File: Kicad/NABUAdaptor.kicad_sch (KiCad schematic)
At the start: 103 parts, among them J1 Conn_01x04, J2 DIN-5_180degree, J3 Conn_01x09, J4 Conn_01x05, U1 74LS164, U10 UA9638CD, U11 UA9637, U12 74LS164, U13 74LS164, U14 74LS04, U15 74LS74, U16 N8X60, U17 2114, U18 2114, U19 LM339, U2 74LS30, U20 74LS164, U21 74LS86, U22 74LS74, U23 74LS00, U24 74LS04, U25 74LS00, U26 74LS74, U27 74LS00, U28 74LS74, U29 74LS74, U3 74LS27, U30 74LS02, U31 MC6805P2, U32 74LS74, U33 74HCU04, U4 74LS164, U5 PAL16R6 (ID PAL), U6 74LS374, U7 74LS373, U8 3k3, U9 TR1865PL, Y1 3.579545MHz

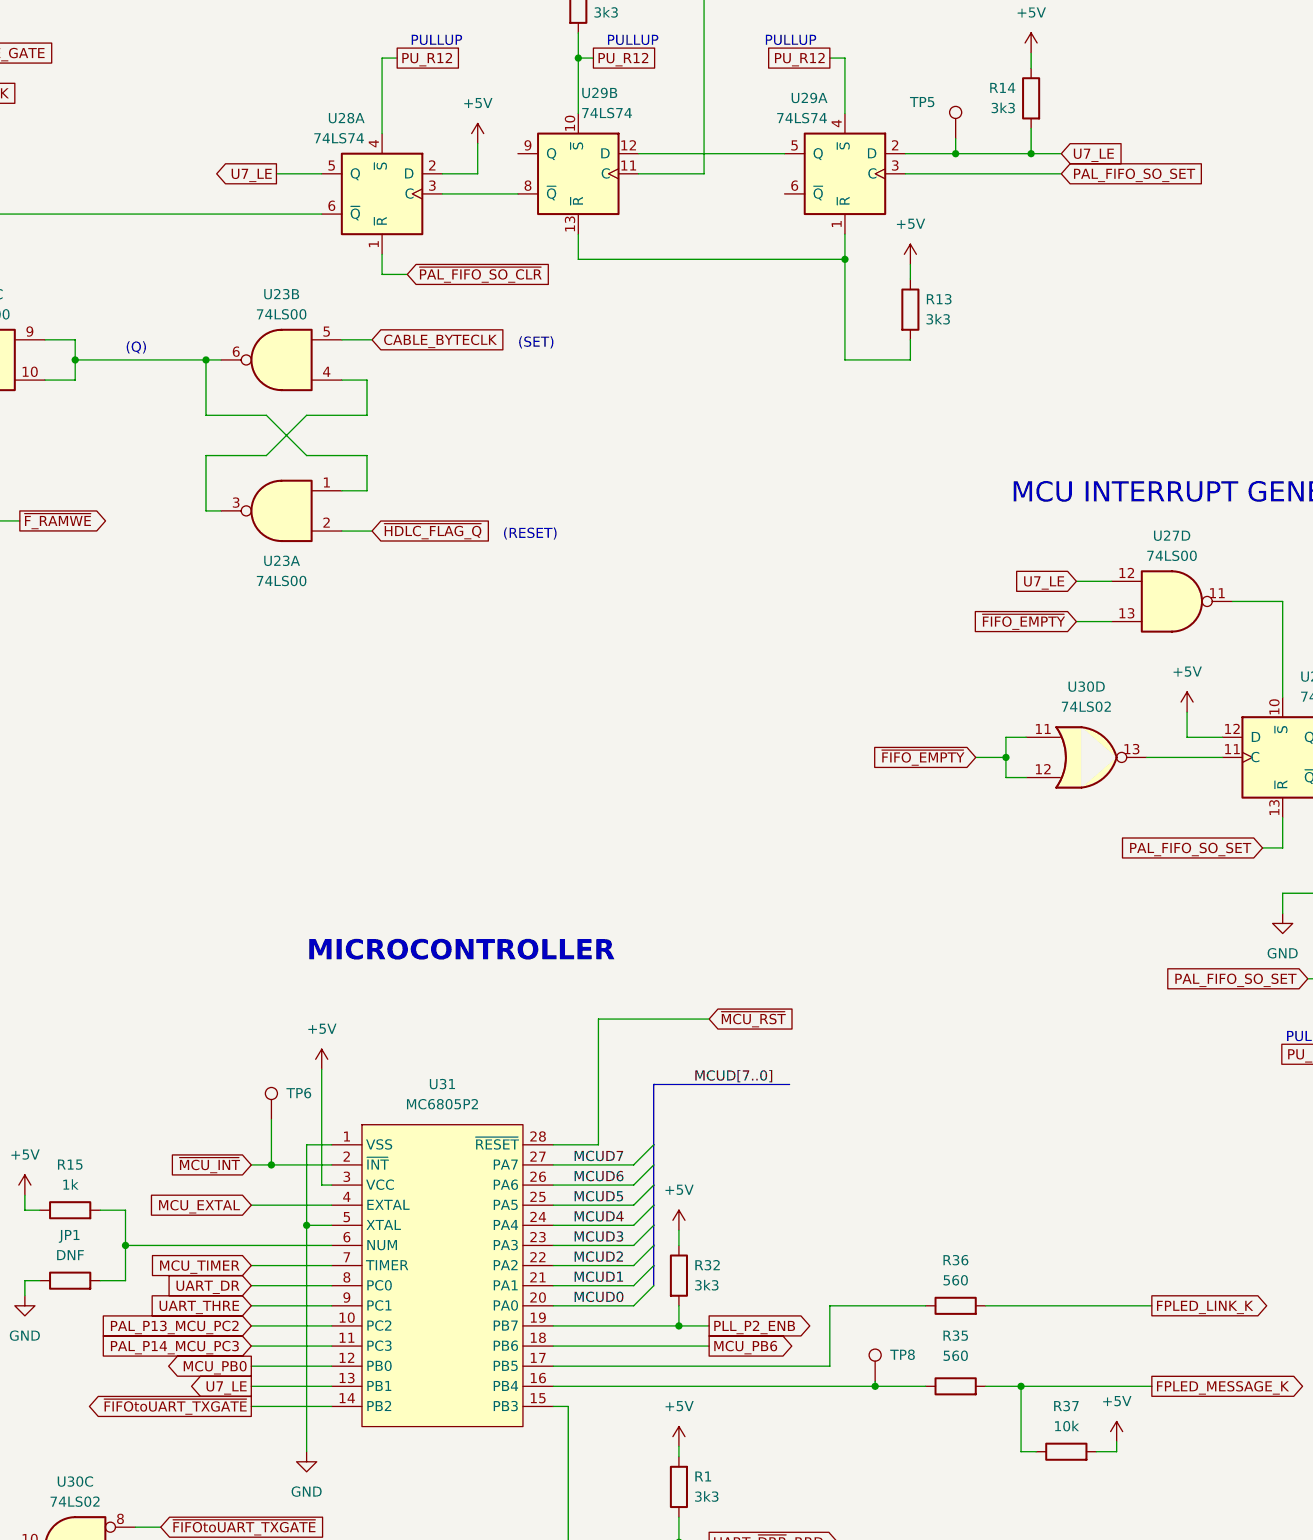
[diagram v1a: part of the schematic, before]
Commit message: schematic: Fix U7 OE wiring
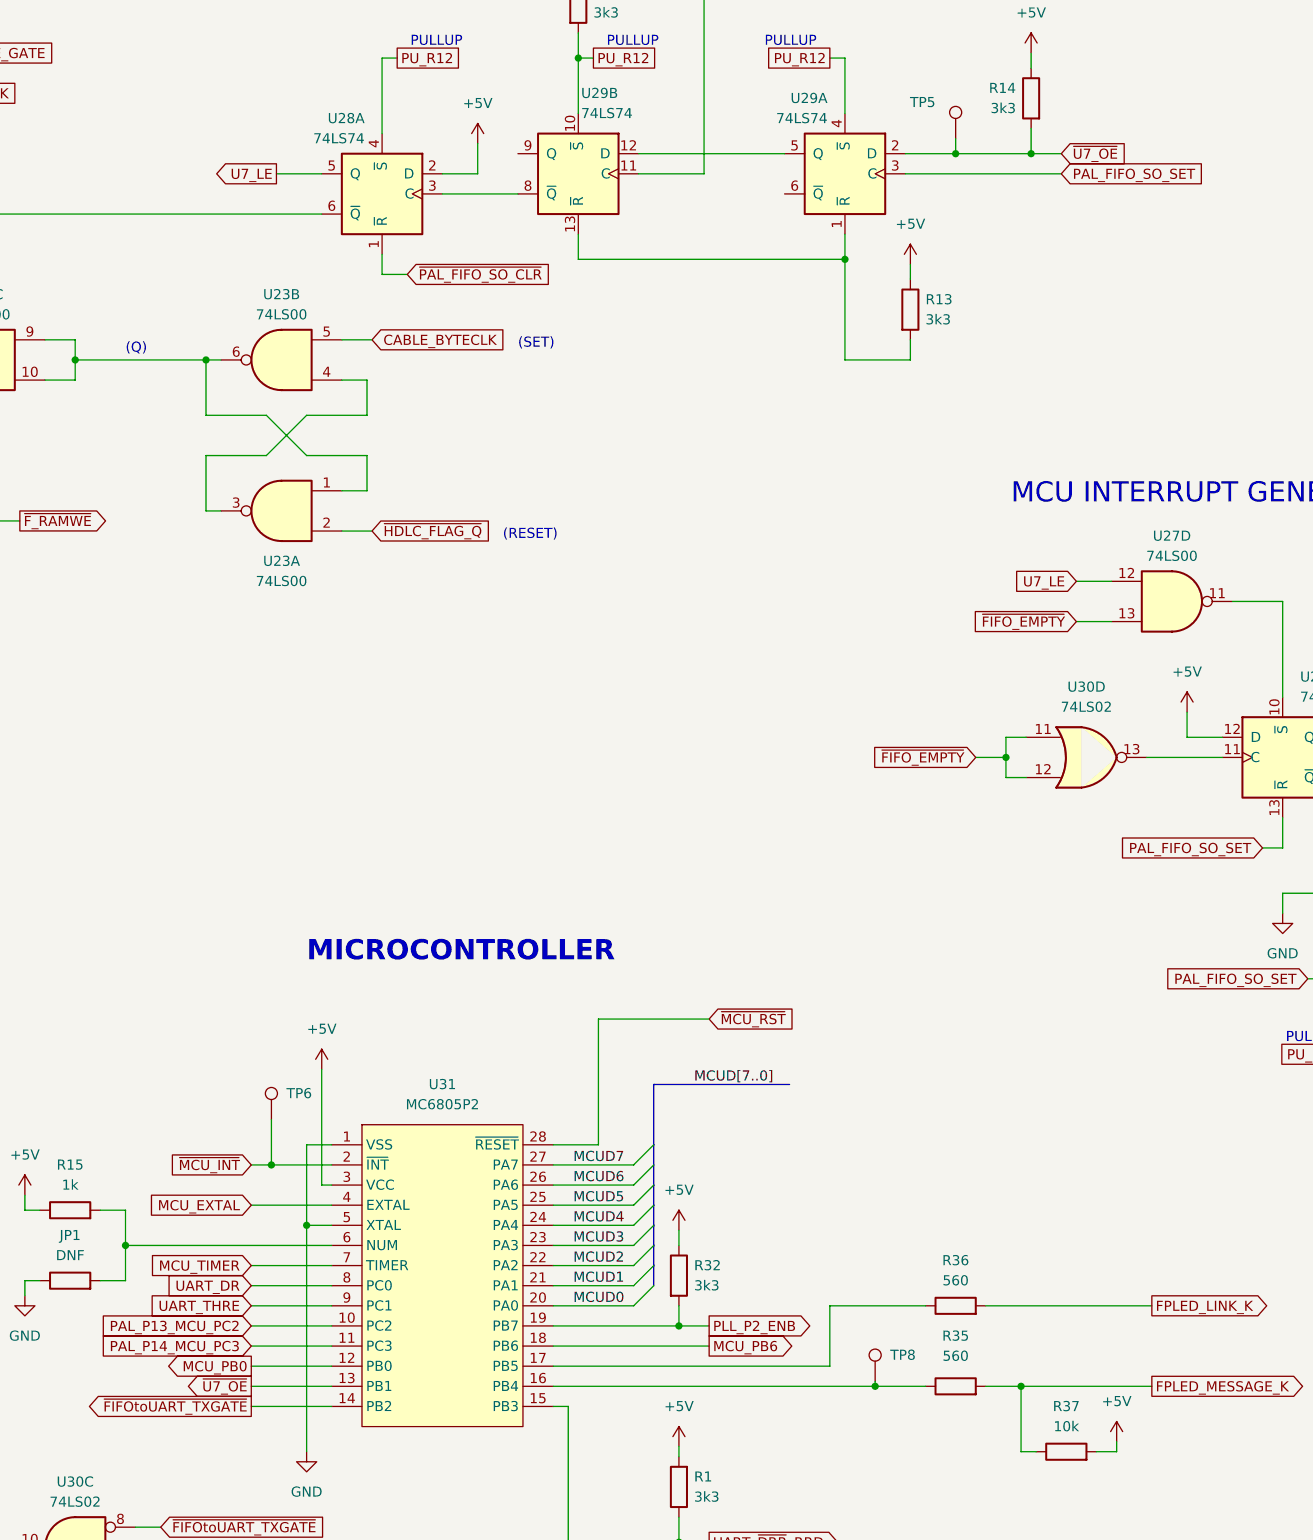
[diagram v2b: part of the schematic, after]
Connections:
- net U7_LE: no longer R14.2, TP5.1, U29.2 (D), U31.13 (PB1)
- net ~{U7_OE}: now also R14.2, TP5.1, U29.2 (D), U31.13 (PB1)
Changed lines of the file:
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@@
     )
   )
-  (global_label "U7_LE" (shape output) (at 419.1 423.545 180) (fields_autoplaced)
+  (global_label "~{U7_OE}" (shape output) (at 419.1 423.545 180) (fields_autoplaced)
     (effects (font (size 1.27 1.27)) (justify right))
-    (property "Intersheetrefs" "${INTERSHEET_REFS}" (at 410.4301 423.545 0)
+    (property "Intersheetrefs" "${INTERSHEET_REFS}" (at 410.1277 423.545 0)
       (effects (font (size 1.27 1.27)) (justify right))
     )
@@
     )
   )
-  (global_label "U7_LE" (shape input) (at 521.335 267.97 0) (fields_autoplaced)
+  (global_label "~{U7_OE}" (shape input) (at 521.335 267.97 0) (fields_autoplaced)
     (effects (font (size 1.27 1.27)) (justify left))
-    (property "Intersheetrefs" "${INTERSHEET_REFS}" (at 530.0049 267.97 0)
+    (property "Intersheetrefs" "${INTERSHEET_REFS}" (at 530.3073 267.97 0)
       (effects (font (size 1.27 1.27)) (justify left))
     )

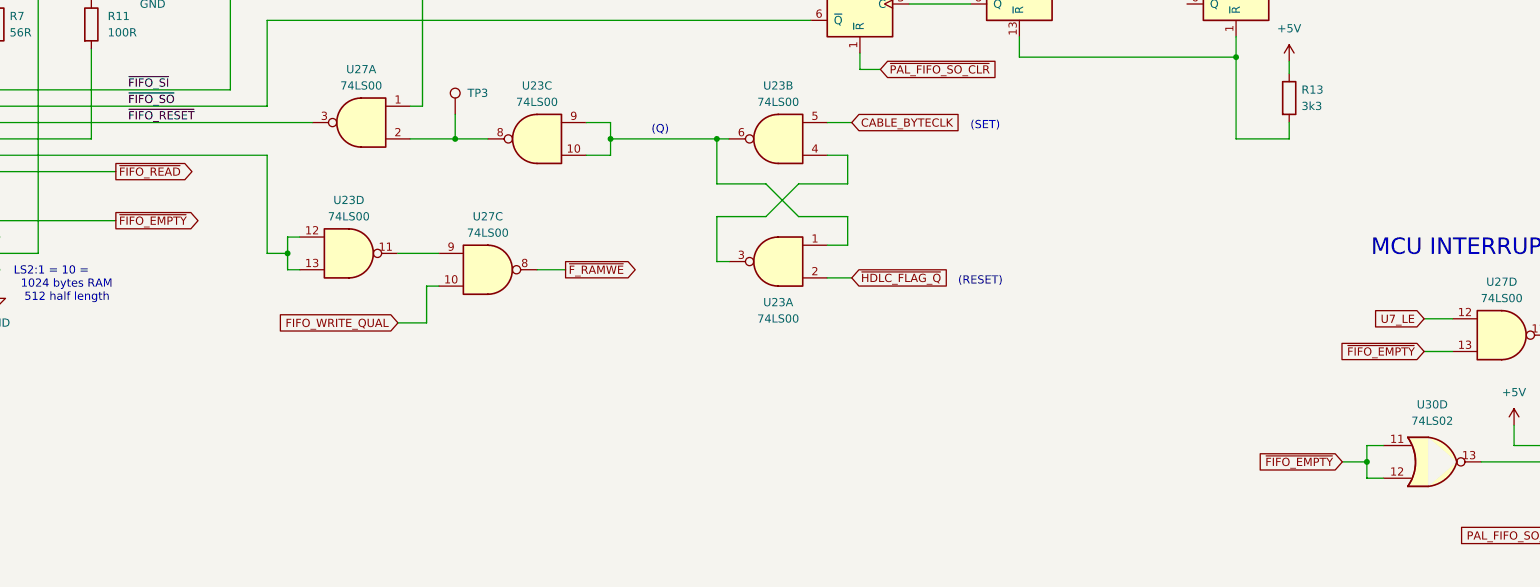
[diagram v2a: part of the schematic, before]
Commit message: schematic: fix signal polarities
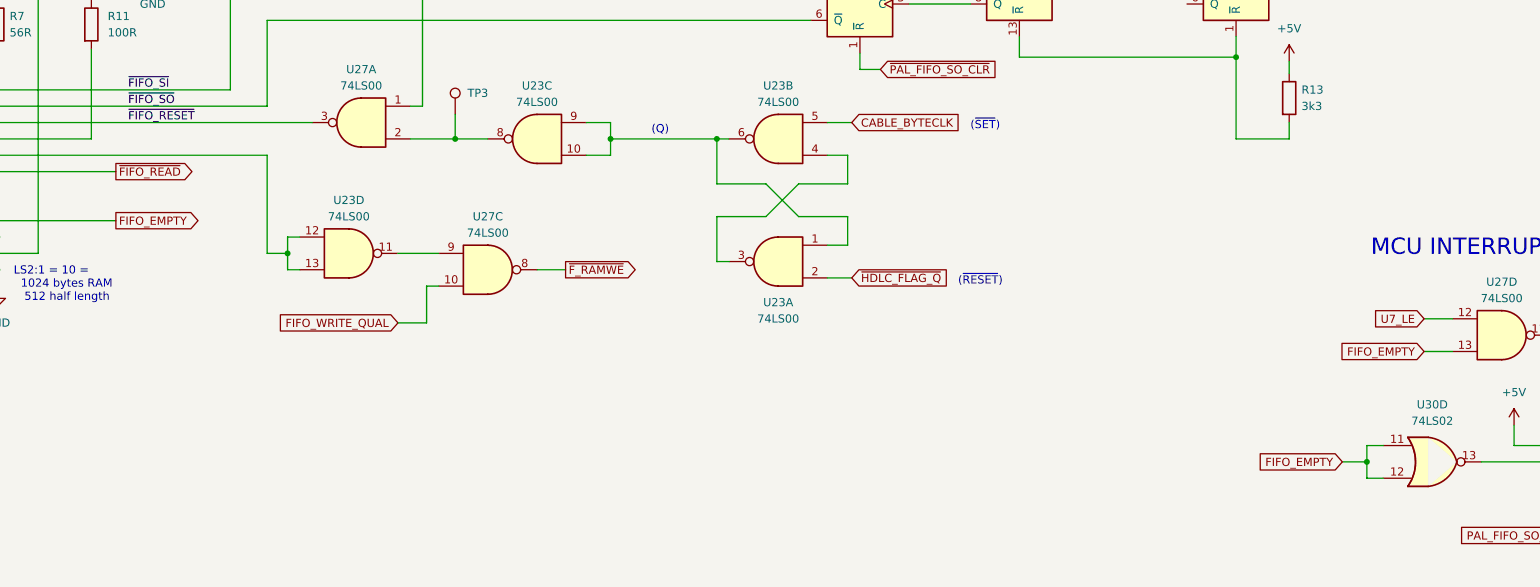
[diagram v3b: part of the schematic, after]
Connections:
- net ~{FIFO_EMPTY} renamed FIFO_EMPTY
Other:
- note added: "(~{RESET})"
- note added: "(~{SET})"
- note removed: "(RESET)"
- note removed: "(SET)"
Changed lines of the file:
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@@
     (effects (font (size 2.54 2.54)) (justify left bottom))
   )
-  (text "(RESET)" (at 450.85 316.865 0)
+  (text "(~{RESET})" (at 450.85 316.865 0)
     (effects (font (size 1.27 1.27)) (justify left bottom))
   )
@@
     (effects (font (size 2.54 2.54) (thickness 0.508) bold) (justify left bottom))
   )
-  (text "(SET)" (at 452.755 292.735 0)
+  (text "(~{SET})" (at 452.755 292.735 0)
     (effects (font (size 1.27 1.27)) (justify left bottom))
   )
@@
     )
   )
-  (global_label "~{FIFO_EMPTY}" (shape input) (at 523.24 327.025 180) (fields_autoplaced)
+  (global_label "FIFO_EMPTY" (shape input) (at 523.24 327.025 180) (fields_autoplaced)
     (effects (font (size 1.27 1.27)) (justify right))
     (property "Intersheetrefs" "${INTERSHEET_REFS}" (at 509.2481 327.025 0)
@@
     )
   )
-  (global_label "~{FIFO_EMPTY}" (shape output) (at 320.04 306.705 0) (fields_autoplaced)
+  (global_label "FIFO_EMPTY" (shape output) (at 320.04 306.705 0) (fields_autoplaced)
     (effects (font (size 1.27 1.27)) (justify left))
     (property "Intersheetrefs" "${INTERSHEET_REFS}" (at 334.0319 306.705 0)
@@
     )
   )
-  (global_label "~{FIFO_EMPTY}" (shape input) (at 510.54 344.17 180) (fields_autoplaced)
+  (global_label "FIFO_EMPTY" (shape input) (at 510.54 344.17 180) (fields_autoplaced)
     (effects (font (size 1.27 1.27)) (justify right))
     (property "Intersheetrefs" "${INTERSHEET_REFS}" (at 496.5481 344.17 0)
